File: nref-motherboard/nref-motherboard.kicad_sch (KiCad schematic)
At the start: 190 parts, among them J1 PWR, J10 1-2199230-6, J10 DISP, J11 BAT1, J12 BAT2, J13 SYSCTL_USB, J16 Conn_01x10_Pin, J17 Conn_01x10_Pin, J17 POWSW, J18 Conn_01x20, J19 SER, J2 Conn_01x12_Pin, J5 SYSCTL, J6 USB_INT1, J8 Conn_01x12_Pin, J9 Conn_01x14_Pin, Q1 NTMFD6H840NL, Q2 NTMFD6H840NL, SW2 RESET, SW4 SW_DIP_x08, U1 reform2-som-connector, U10 BQ25756RRVR, U10 W25Q32JVSS, U11 LM62460, U2 MAX1837EUT33+T, U26 74HC573, U5 LM62460, U7 USB2514B_Bi, U8 RP2040, Y2 12MHz 18pF, Y2 24MHz

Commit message: motherboard: schematic done for d-1?
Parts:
- added C75: 10uF, Capacitor_SMD:C_0603_1608Metric, symbol Device:C_Small
- added D10, D11: LED_RED, LED_SMD:LED_0603_1608Metric, symbol Device:LED_Small
- added D4: LED_RED, LED_SMD:LED_0402_1005Metric, symbol Device:LED_Small
- added R68: 0, Resistor_SMD:R_0402_1005Metric, symbol Device:R_Small
- added R69: 1M, Resistor_SMD:R_0402_1005Metric, symbol Device:R_Small
- added R70: 5.24k, Resistor_SMD:R_0402_1005Metric, symbol Device:R_Small
- added R71, R72, R73, R74: 10k, Resistor_SMD:R_0402_1005Metric, symbol Device:R_Small
- added R75, R76: 100k, Resistor_SMD:R_0402_1005Metric, symbol Device:R_Small
- added TH1: 10k, Resistor_SMD:R_0402_1005Metric, symbol Device:Thermistor_NTC
- R15, R35, R4, R5: value 50k -> 47k
- R45, R46, R47, R48: footprint (none) -> Resistor_SMD:R_0402_1005Metric
- R60: value 10k -> 30.31k
- R62, R63: value TODO -> 0
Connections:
- net +3V3: now also R69.2, R75.2; no longer U5.10 (RESET)
- net +5V: now also R76.2; no longer U11.10 (RESET)
- net GND: now also R60.1, C75.2, TH1.1; no longer R60.2
- net PCIE1_RESETn: no longer J10.50
- net PCIE2_RESETn: now also J10.50
- net REGN: now also D10.2 (A), D11.2 (A), D4.2 (A), R70.2
- net STANDBY_3V3: now also R74.2
- net ~{USBH_RESET}: now also R68.1
- net ~{CHRG_CE}: now reaches U8.31 (GPIO20)
- net ~{CHRG_CE}: now also U10.7 (~{CE}), R74.1
- net CHRG_STAT1: now reaches U10.4 (STAT1)
- net CHRG_STAT1: now also R73.2
- net CHRG_STAT2: now reaches U10.5 (STAT2)
- net CHRG_STAT2: now also R72.2
- net ~{CHRG_PG}: now reaches U10.6 (~{PG})
- net ~{CHRG_PG}: now also R71.2
- net at U10.8 (TS): now also R60.2, R70.1, TH1.2; no longer R60.1
- net USB_HUB_RESET: no longer names the net of U7.26 (RESET_N)
- net USB_HUB_RESET: now also C75.1, R68.2, R69.1
- new net: R75.1, U5.10 (RESET)
- new net: R76.1, U11.10 (RESET)
- new net: D4.1 (K), R71.1
- new net: D11.1 (K), R73.1
- new net: D10.1 (K), R72.1
- no-connect marks 102 -> 103
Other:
- note added: "Control DIP Switch Array"
- note added: "Main/Charge Buck Boost"
- note added: "required on the board: - [x] reform slot - [x] M.2 SSD slot (can it fit underneath?) - [x] 3V3 dcdc - [x] sysctl (next-gen rpi2040?) - [x] FPC or JST-SH headers going to ports off board: - [ ] USB-C FUSB - [ ] DAC/ADC"
- note removed: "TODO"
- note removed: "TODO: 10k thermistor"
- note removed: "TODO: unconnected? RC?"
- note removed: "TODO: why not 47k?"
- note removed: "required on the board: - [x] reform slot - [x] M.2 SSD slot (can it fit underneath?) - [ ] USB-C to 5V power - [x] 3V3 dcdc - [ ] 1v8 dcdc or LDO - [x] sysctl (next-gen rpi2040?) - [x] FPC or JST-SH headers going to ports - [ ] DAC/ADC"
- moved on the sheet: C109, C11, C124, C126, C13, C14, C15, C16, C17, C2, C22, C24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

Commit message: mb: swap some intersecting connectors; more routing
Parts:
- J16, J17: footprint Connector_JST:JST_SH_SM10B-SRSS-TB_1x10-1MP_P1.00mm_Horizontal -> Connector_FFC-FPC:Hirose_FH12-10S-0.5SH_1x10-1MP_P0.50mm_Horizontal
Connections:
- net GND: now also J16.4 (Pin_4); no longer J16.7 (Pin_7)
- net SD_CLK: now also J16.3 (Pin_3); no longer J16.8 (Pin_8)
- net SD_CMD: now also J16.5 (Pin_5); no longer J16.6 (Pin_6)
- net SD_D0: now also J16.9 (Pin_9); no longer J16.2 (Pin_2)
- net SD_D1: now also J16.8 (Pin_8); no longer J16.3 (Pin_3)
- net SD_D2: now also J16.7 (Pin_7); no longer J16.4 (Pin_4)
- net SD_D3: now also J16.6 (Pin_6); no longer J16.5 (Pin_5)
- net SD_DET: now also J16.2 (Pin_2); no longer J16.9 (Pin_9)
- net 1V1_ENABLE: no longer names the net of U8.35 (GPIO23)
- net RP_UART2_RX: no longer names the net of U1.30 (UART3_TXD)
- net RP_UART2_RX: no longer U8.16 (GPIO13)
- net RP_UART2_TX: no longer names the net of U1.32 (UART3_RXD)
- net RP_UART2_TX: no longer U8.15 (GPIO12)
- no-connect marks 103 -> 108
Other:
- note added: "TODO: unaccounted for!"
- note added: "UART 2 (unused)"
- note added: "connected to LPC on other Reforms"
- note removed: "UART to SOC"
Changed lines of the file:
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@@
 	)
 	(no_connect
+		(at 166.37 113.03)
+	)
+	(no_connect
 		(at 111.76 171.45)
 	)
@@
 	)
 	(no_connect
+		(at 758.19 266.7)
+	)
+	(no_connect
 		(at 154.94 115.57)
 	)
@@
 	)
 	(no_connect
+		(at 758.19 269.24)
+	)
+	(no_connect
 		(at 111.76 255.27)
 	)
@@
 	)
 	(no_connect
+		(at 741.68 294.64)
+	)
+	(no_connect
 		(at 111.76 209.55)
 	)
@@
 	)
 	(no_connect
+		(at 166.37 110.49)
+	)
+	(no_connect
 		(at 111.76 250.19)
 	)
@@
 	(wire
 		(pts
-			(xy 741.68 294.64) (xy 760.73 294.64)
-		)
-		(stroke
-			(width 0)
-			(type default)
-		)
-	)
-	(wire
-		(pts
 			(xy 453.39 232.41) (xy 453.39 236.22)
 		)
@@
 	(wire
 		(pts
+			(xy 82.55 469.9) (xy 100.33 469.9)
+		)
+		(stroke
+			(width 0)
+			(type default)
+		)
+	)
+	(wire
+		(pts
 			(xy 480.06 113.03) (xy 487.68 113.03)
 		)
@@
 	(wire
 		(pts
-			(xy 100.33 477.52) (xy 100.33 485.14)
+			(xy 100.33 469.9) (xy 100.33 485.14)
 		)
 		(stroke
@@
 	(wire
 		(pts
-			(xy 82.55 477.52) (xy 100.33 477.52)
-		)
-		(stroke
-			(width 0)
-			(type default)
-		)
-	)
-	(wire
-		(pts
 			(xy 111.76 229.87) (xy 85.09 229.87)
 		)
@@
 		)
 	)
-	(text "UART to SOC"
+	(text "UART 2 (unused)"
 		(exclude_from_sim no)
-		(at 774.7 269.24 0)
+		(at 759.46 269.24 0)
 		(effects
 			(font
@@
 		)
 	)
+	(text "TODO: unaccounted for!"
+		(exclude_from_sim no)
+		(at 849.63 281.94 0)
+		(effects
+			(font
+				(size 1.27 1.27)
+			)
+			(justify left bottom)
+		)
+	)
 	(text "MAX 24V"
 		(exclude_from_sim no)
@@
 		)
 	)
+	(text "connected to LPC on other Reforms"
+		(exclude_from_sim no)
+		(at 185.42 111.76 0)
+		(effects
+			(font
+				(size 1.27 1.27)
+			)
+		)
+	)
 	(text "Control DIP Switch Array"
 		(exclude_from_sim no)
@@
 	(global_label "SD_D1"
 		(shape bidirectional)
-		(at 82.55 467.36 0)
+		(at 82.55 480.06 0)
 		(fields_autoplaced yes)
 		(effects
@@
 		)
 		(property "Intersheetrefs" "${INTERSHEET_REFS}"
-			(at 90.8009 467.2806 0)
+			(at 90.8009 480.1394 0)
 			(effects
 				(font
@@
 		)
 	)
+	(global_label "USB_SRC_EN"
+		(shape output)
+		(at 853.44 285.75 0)
+		(fields_autoplaced yes)
+		(effects
+			(font
+				(size 1.27 1.27)
+			)
+			(justify left)
+		)
+		(property "Intersheetrefs" "${INTERSHEET_REFS}"
+			(at 867.7385 285.6706 0)
+			(effects
+				(font
+					(size 1.27 1.27)
+				)
+				(justify left)
+				(hide yes)
+			)
+		)
+	)
 	(global_label "HDMI_TX1P"
 		(shape input)
@@
 		)
 	)
-	(global_label "RP_UART2_RX"
-		(shape output)
-		(at 166.37 110.49 0)
-		(fields_autoplaced yes)
-		(effects
-			(font
-				(size 1.27 1.27)
-			)
-			(justify left)
-		)
-		(property "Intersheetrefs" "${INTERSHEET_REFS}"
-			(at 181.5152 110.4106 0)
-			(effects
-				(font
-					(size 1.27 1.27)
-				)
-				(justify left)
-				(hide yes)
-			)
-		)
-	)
 	(global_label "PCIE2_CLK_N"
 		(shape input)
@@
 	(global_label "SD_CMD"
 		(shape output)
-		(at 82.55 474.98 0)
+		(at 82.55 472.44 0)
 		(fields_autoplaced yes)
 		(effects
@@
 		)
 		(property "Intersheetrefs" "${INTERSHEET_REFS}"
-			(at 92.3128 474.9006 0)
+			(at 92.3128 472.5194 0)
 			(effects
 				(font
@@
 	(global_label "SD_CLK"
 		(shape output)
-		(at 82.55 480.06 0)
+		(at 82.55 467.36 0)
 		(fields_autoplaced yes)
 		(effects
@@
 		)
 		(property "Intersheetrefs" "${INTERSHEET_REFS}"
-			(at 91.8894 479.9806 0)
+			(at 91.8894 467.4394 0)
 			(effects
 				(font
@@
 		)
 	)
+	(global_label "RP_FUSB_INT"
+		(shape input)
+		(at 853.44 288.29 0)
+		(fields_autoplaced yes)
+		(effects
+			(font
+				(size 1.27 1.27)
+			)
+			(justify left)
+		)
+		(property "Intersheetrefs" "${INTERSHEET_REFS}"
+			(at 868.0409 288.2106 0)
+			(effects
+				(font
+					(size 1.27 1.27)
+				)
+				(justify left)
+				(hide yes)
+			)
+		)
+	)
 	(global_label "IMX_UART1_RX"
 		(shape input)
@@
 	(global_label "SD_D0"
 		(shape bidirectional)
-		(at 82.55 464.82 0)
+		(at 82.55 482.6 0)
 		(fields_autoplaced yes)
 		(effects
@@
 		)
 		(property "Intersheetrefs" "${INTERSHEET_REFS}"
-			(at 90.8009 464.7406 0)
+			(at 90.8009 482.6794 0)
 			(effects
 				(font
@@
 	(global_label "SD_D3"
 		(shape bidirectional)
-		(at 82.55 472.44 0)
+		(at 82.55 474.98 0)
 		(fields_autoplaced yes)
 		(effects
@@
 		)
 		(property "Intersheetrefs" "${INTERSHEET_REFS}"
-			(at 90.8009 472.3606 0)
+			(at 90.8009 475.0594 0)
 			(effects
 				(font
@@
 	(global_label "SD_D2"
 		(shape bidirectional)
-		(at 82.55 469.9 0)
+		(at 82.55 477.52 0)
 		(fields_autoplaced yes)
 		(effects
@@
 		)
 		(property "Intersheetrefs" "${INTERSHEET_REFS}"
-			(at 90.8009 469.8206 0)
+			(at 90.8009 477.5994 0)
 			(effects
 				(font
@@
 		)
 	)
-	(global_label "1V1_ENABLE"
-		(shape output)
-		(at 760.73 294.64 0)
-		(fields_autoplaced yes)
-		(effects
-			(font
-				(size 1.27 1.27)
-			)
-			(justify left)
-		)
-		(property "Intersheetrefs" "${INTERSHEET_REFS}"
-			(at 774.5447 294.5606 0)
-			(effects
-				(font
-					(size 1.27 1.27)
-				)
-				(justify left)
-				(hide yes)
-			)
-		)
-	)
 	(global_label "PCIE1_RESETn"
 		(shape output)
@@
 		)
 	)
-	(global_label "RP_UART2_RX"
-		(shape input)
-		(at 758.19 269.24 0)
-		(fields_autoplaced yes)
-		(effects
-			(font
-				(size 1.27 1.27)
-			)
-			(justify left)
-		)
-		(property "Intersheetrefs" "${INTERSHEET_REFS}"
-			(at 773.3352 269.1606 0)
-			(effects
-				(font
-					(size 1.27 1.27)
-				)
-				(justify left)
-				(hide yes)
-			)
-		)
-	)
 	(global_label "RP_SCL0"
 		(shape output)
@@
 		)
 	)
-	(global_label "RP_UART2_TX"
-		(shape input)
-		(at 166.37 113.03 0)
-		(fields_autoplaced yes)
-		(effects
-			(font
-				(size 1.27 1.27)
-			)
-			(justify left)
-		)
-		(property "Intersheetrefs" "${INTERSHEET_REFS}"
-			(at 181.2128 112.9506 0)
-			(effects
-				(font
-					(size 1.27 1.27)
-				)
-				(justify left)
-				(hide yes)
-			)
-		)
-	)
 	(global_label "UART2_TX"
 		(shape input)
@@
 	(global_label "SD_DET"
 		(shape input)
-		(at 82.55 482.6 0)
+		(at 82.55 464.82 0)
 		(fields_autoplaced yes)
 		(effects
@@
 		)
 		(property "Intersheetrefs" "${INTERSHEET_REFS}"
-			(at 91.708 482.6794 0)
+			(at 91.708 464.7406 0)
 			(effects
 				(font
@@
 		)
 	)
-	(global_label "RP_UART2_TX"
-		(shape output)
-		(at 758.19 266.7 0)
-		(fields_autoplaced yes)
-		(effects
-			(font
-				(size 1.27 1.27)
-			)
-			(justify left)
-		)
-		(property "Intersheetrefs" "${INTERSHEET_REFS}"
-			(at 773.0328 266.6206 0)
-			(effects
-				(font
-					(size 1.27 1.27)
-				)
-				(justify left)
-				(hide yes)
-			)
-		)
-	)
 	(global_label "PCIE2_TX2_P"
 		(shape input)
@@
 			)
 		)
-		(property "Footprint" "Connector_JST:JST_SH_SM10B-SRSS-TB_1x10-1MP_P1.00mm_Horizontal"
+		(property "Footprint" "Connector_FFC-FPC:Hirose_FH12-10S-0.5SH_1x10-1MP_P0.50mm_Horizontal"
 			(at 119.38 472.44 0)
 			(effects
@@
 			)
 		)
-		(property "Footprint" "Connector_JST:JST_SH_SM10B-SRSS-TB_1x10-1MP_P1.00mm_Horizontal"
+		(property "Footprint" "Connector_FFC-FPC:Hirose_FH12-10S-0.5SH_1x10-1MP_P0.50mm_Horizontal"
 			(at 77.47 472.44 0)
 			(effects

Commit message: mb routing snapshot
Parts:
- D4: footprint LED_SMD:LED_0402_1005Metric -> LED_SMD:LED_0603_1608Metric
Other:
- note added: "could we do this as I2C GPIO on power input board?"
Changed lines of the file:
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@@
 	(text "TODO: unaccounted for!"
 		(exclude_from_sim no)
-		(at 849.63 281.94 0)
+		(at 849.63 275.59 0)
 		(effects
 			(font
@@
 		)
 	)
+	(text "could we do this as I2C GPIO on power input board?"
+		(exclude_from_sim no)
+		(at 849.63 280.67 0)
+		(effects
+			(font
+				(size 1.27 1.27)
+			)
+			(justify left bottom)
+		)
+	)
 	(text "TODO: more cap?"
 		(exclude_from_sim no)
@@
 			)
 		)
-		(property "Footprint" "LED_SMD:LED_0402_1005Metric"
+		(property "Footprint" "LED_SMD:LED_0603_1608Metric"
 			(at 528.32 537.21 90)
 			(effects

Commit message: mb routing snapshot
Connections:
- net GND: now also C11.2, C14.2, C16.2, C57.2, C6.2
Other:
- note added: "TODO: connect to rp2040?"
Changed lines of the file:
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@@
 	(wire
 		(pts
+			(xy 525.78 165.1) (xy 525.78 163.83)
+		)
+		(stroke
+			(width 0)
+			(type default)
+		)
+	)
+	(wire
+		(pts
 			(xy 110.49 120.65) (xy 111.76 120.65)
 		)
@@
 		)
 	)
+	(text "TODO: connect to rp2040?"
+		(exclude_from_sim no)
+		(at 50.8 189.23 0)
+		(effects
+			(font
+				(size 1.27 1.27)
+			)
+		)
+	)
 	(text "PERn1"
 		(exclude_from_sim no)
@@
 					(unit 1)
 				)
+			)
+		)
+	)
+	(symbol
+		(lib_id "power:GND")
+		(at 525.78 165.1 0)
+		(unit 1)
+		(exclude_from_sim no)
+		(in_bom yes)
+		(on_board yes)
+		(dnp no)
+		(property "Reference" "#PWR077"
+			(at 525.78 171.45 0)
+			(effects
+				(font
+					(size 1.27 1.27)
+				)
+				(hide yes)
+			)
+		)
+		(property "Value" "GND"
+			(at 525.78 168.91 0)
+			(effects
+				(font
+					(size 1.27 1.27)
+				)
+			)
+		)
+		(property "Footprint" ""
+			(at 525.78 165.1 0)
+			(effects
+				(font
+					(size 1.27 1.27)
+				)
+				(hide yes)
+			)
+		)
+		(property "Datasheet" ""
+			(at 525.78 165.1 0)
+			(effects
+				(font
+					(size 1.27 1.27)
+				)
+				(hide yes)
+			)
+		)
+		(property "Description" ""
+			(at 525.78 165.1 0)
+			(effects
+				(font
+					(size 1.27 1.27)
+				)
+				(hide yes)
+			)
+		)
+		(pin "1"
+		)
+		(instances
+			(project "nref-motherboard"
+				(path "/a432b2af-5748-42a5-94fe-8be4ed1e5510"
+					(reference "#PWR077")
+					(unit 1)
+				)

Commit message: mb routing snapshot
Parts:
- removed R66, R67: 0, Resistor_SMD:R_0402_1005Metric, symbol Device:R_Small
- added C74, C76: 18pF, Capacitor_SMD:C_0402_1005Metric, symbol Device:C_Small
- added C77: 0.1uF, Capacitor_SMD:C_0402_1005Metric, symbol Device:C_Small
- added C78: 4.7uF, Capacitor_SMD:C_0402_1005Metric, symbol Device:C_Small
- added R77, R78: 0, Resistor_SMD:R_0402_1005Metric, symbol Device:R_Small
- added U4: Si52111-B5, Package_SO:TSSOP-8_4.4x3mm_P0.65mm, symbol Si52111-B5:Si52111-B5
- added Y3: 25MHz, Crystal:Crystal_SMD_3225-4Pin_3.2x2.5mm, symbol Device:Crystal_GND24_Small
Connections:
- net IMX_UART1_RX is gone; now on net UART1_RX: U1.126 (UART1_RXD)
- net IMX_UART1_TX is gone; now on net UART1_TX: U1.128 (UART1_TXD)
- net IMX_UART2_RX is gone; now on net UART2_RX: U1.122 (UART2_RXD)
- net IMX_UART2_TX is gone; now on net UART2_TX: U1.124 (UART2_TXD)
- net VBUS_5V is gone; now on net +5V: J2.2 (Pin_2), J2.3 (Pin_3), J8.2 (Pin_2), J8.3 (Pin_3)
- net +3V3: now also C77.1, C78.1, U4.1 (VDD)
- net GND: now also C74.2, C76.2, C77.2, C78.2, R77.2, R78.2, U4.4 (VSS), Y3.2, Y3.4; no longer U10.10 (ILIM_HIZ), U10.9 (ICHG)
- net PCIE2_CLK2_N: now also J10.53, R199.2
- net PCIE2_CLK2_P: now also J10.55, R198.2
- net PCIE2_CLK_N: now also U4.6 (DIFF1_N); no longer J10.53, R199.2
- net PCIE2_CLK_P: now also U4.5 (DIFF1_P); no longer J10.55, R198.2
- new net: C76.1, U4.2 (XOUT), Y3.3
- new net: R77.1, U10.10 (ILIM_HIZ)
- new net: C74.1, U4.3 (XIN), Y3.1
- new net: R78.1, U10.9 (ICHG)
- no-connect marks 108 -> 110
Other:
- note added: "TODO: actual ICHG/ILIM resistor values?"
- note added: "buffered clock from module coming back"
- note added: "going into clock buffer on module"
- note added: "lets do them as I2C GPIO on power input board"
- note removed: "TODO: ICHG resistor for charge current limiting"
- note removed: "TODO: clock synth! but for now we just recycle PCIe 1's clock"
- note removed: "TODO: not needed?"
- note removed: "could we do this as I2C GPIO on power input board?"

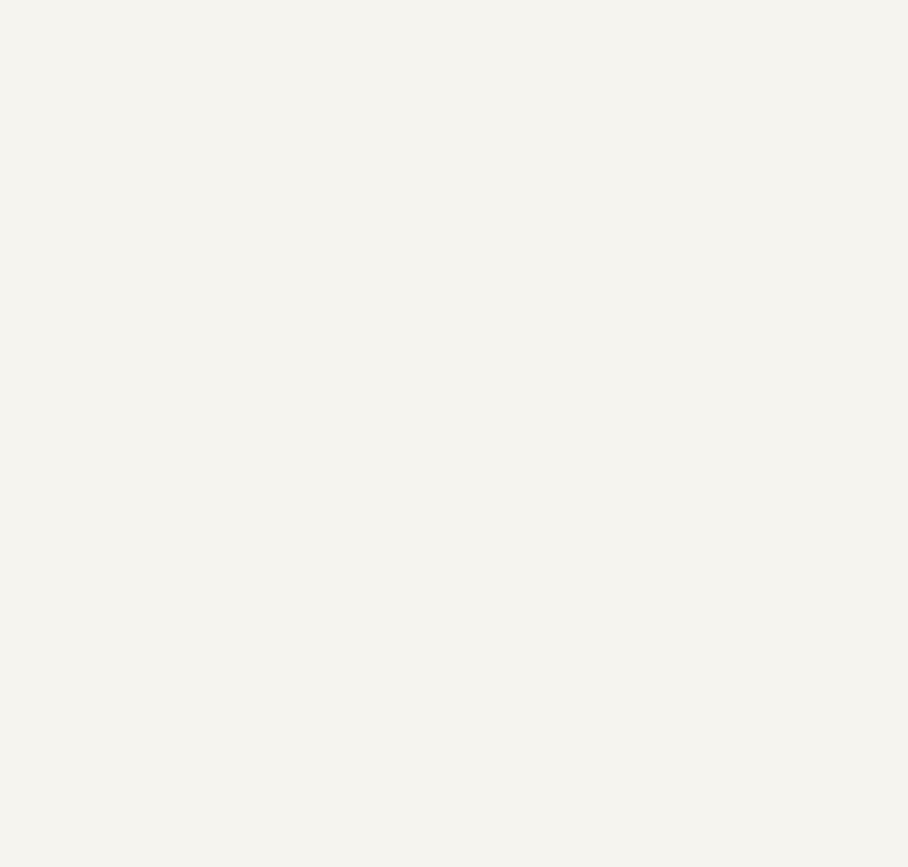
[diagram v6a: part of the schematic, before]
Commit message: mb silkscreen cleaned up
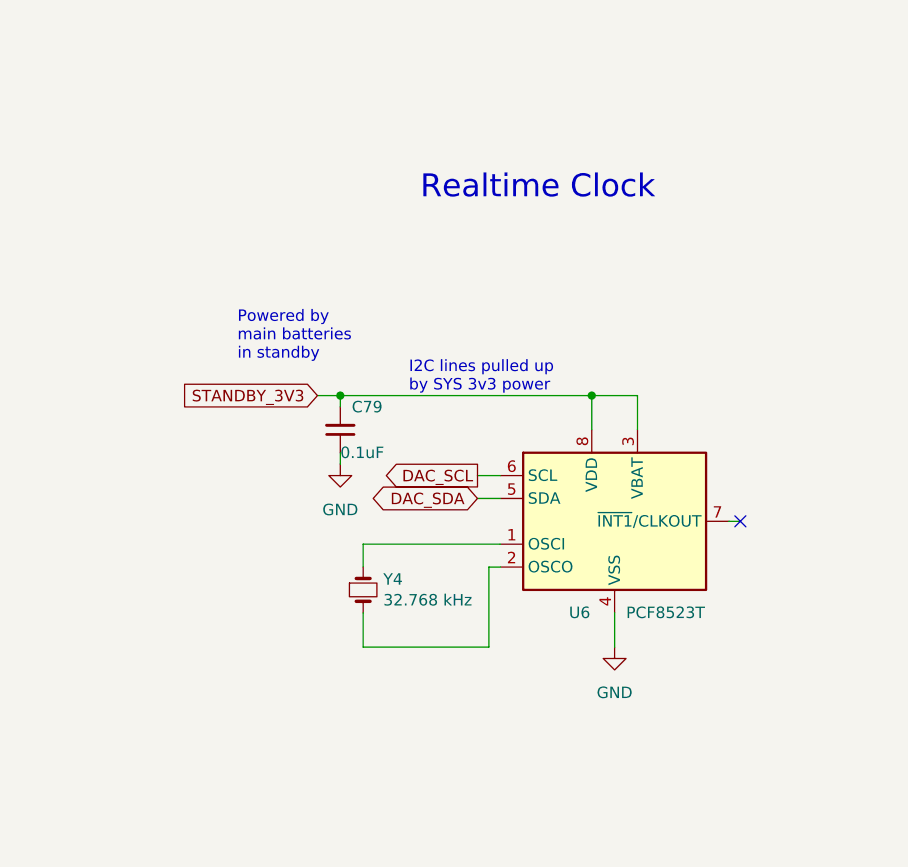
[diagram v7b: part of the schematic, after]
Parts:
- added C79: 0.1uF, Capacitor_SMD:C_0402_1005Metric, symbol Device:C_Small
- added U6: PCF8523T, Package_SO:SOIC-8_3.9x4.9mm_P1.27mm, symbol Timer_RTC:PCF8523T
- added Y4: 32.768 kHz, Crystal:Crystal_SMD_3215-2Pin_3.2x1.5mm, symbol Device:Crystal_Small
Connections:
- net DAC_SCL: now also U6.6 (SCL)
- net DAC_SDA: now also U6.5 (SDA)
- net GND: now also C79.1, U6.4 (VSS)
- net STANDBY_3V3: now also C79.2, U6.3 (VBAT), U6.8 (VDD)
- new net: U6.1 (OSCI), Y4.1
- new net: U6.2 (OSCO), Y4.2
- no-connect marks 110 -> 111
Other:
- note added: "I2C lines pulled up by SYS 3v3 power"
- note added: "Powered by main batteries in standby"
- note added: "Realtime Clock"

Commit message: motherboard d-1 production snapshot
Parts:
- added H6: LOGO, footprints:nref-reflex-logo, symbol Mechanical:MountingHole
- added H7: BADGE, footprints:nref-motherboard-badge, symbol Mechanical:MountingHole
- added TP1, TP2, TP3, TP4: TestPoint, TestPoint:TestPoint_Pad_1.0x1.0mm, symbol Connector:TestPoint
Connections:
- net HDMI_AUXN: now also TP4.1
- net HDMI_AUXP: now also TP3.1
- net USB2D_DN: now reaches U7.8 (USBDM_DN4/PRT_DIS_M4)
- net USB2D_DN: now also TP2.1
- net USB2D_DP: now reaches U7.9 (USBDP_DN4/PRT_DIS_P4)
- net USB2D_DP: now also TP1.1
- no-connect marks 111 -> 109
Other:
- note added: "TODO: AUX for DP?"
- note added: "extra internal usb"
- note removed: "TODO: extra usb"
